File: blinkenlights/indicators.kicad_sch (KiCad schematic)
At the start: 45 parts

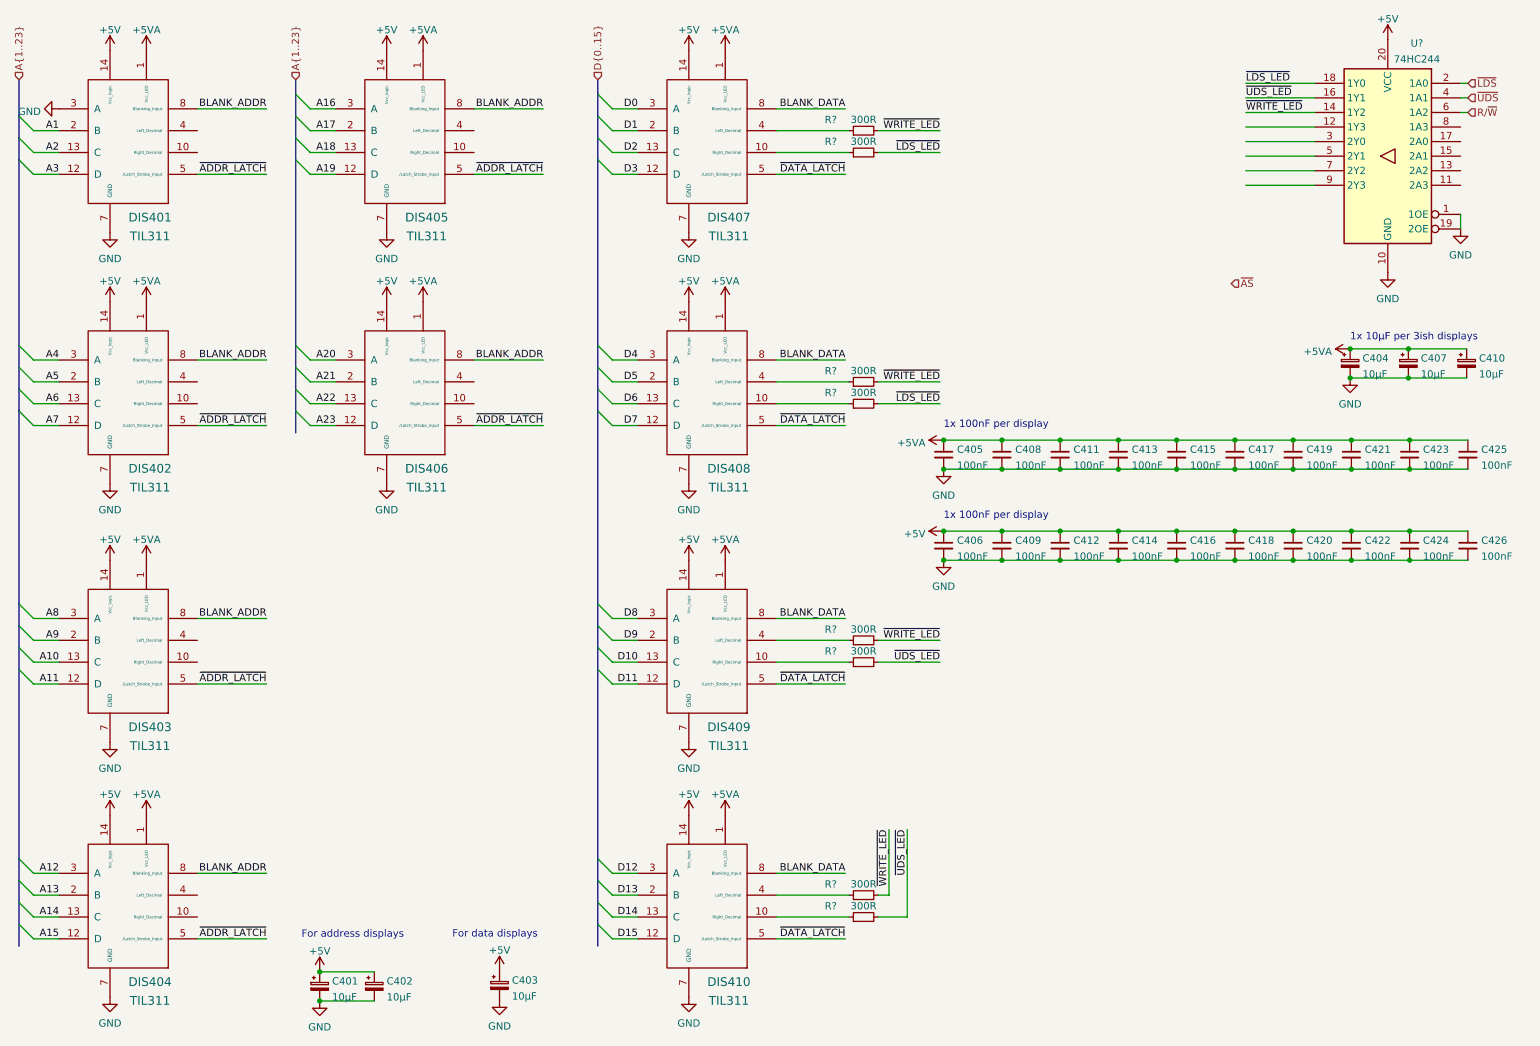
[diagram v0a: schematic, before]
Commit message: Start work on blinkenlights pcb
- This is mostly for the general layout and physical size of the board;
  all the components are placed on the back so the pin numbers will line
  up properly on the DIN connectors.
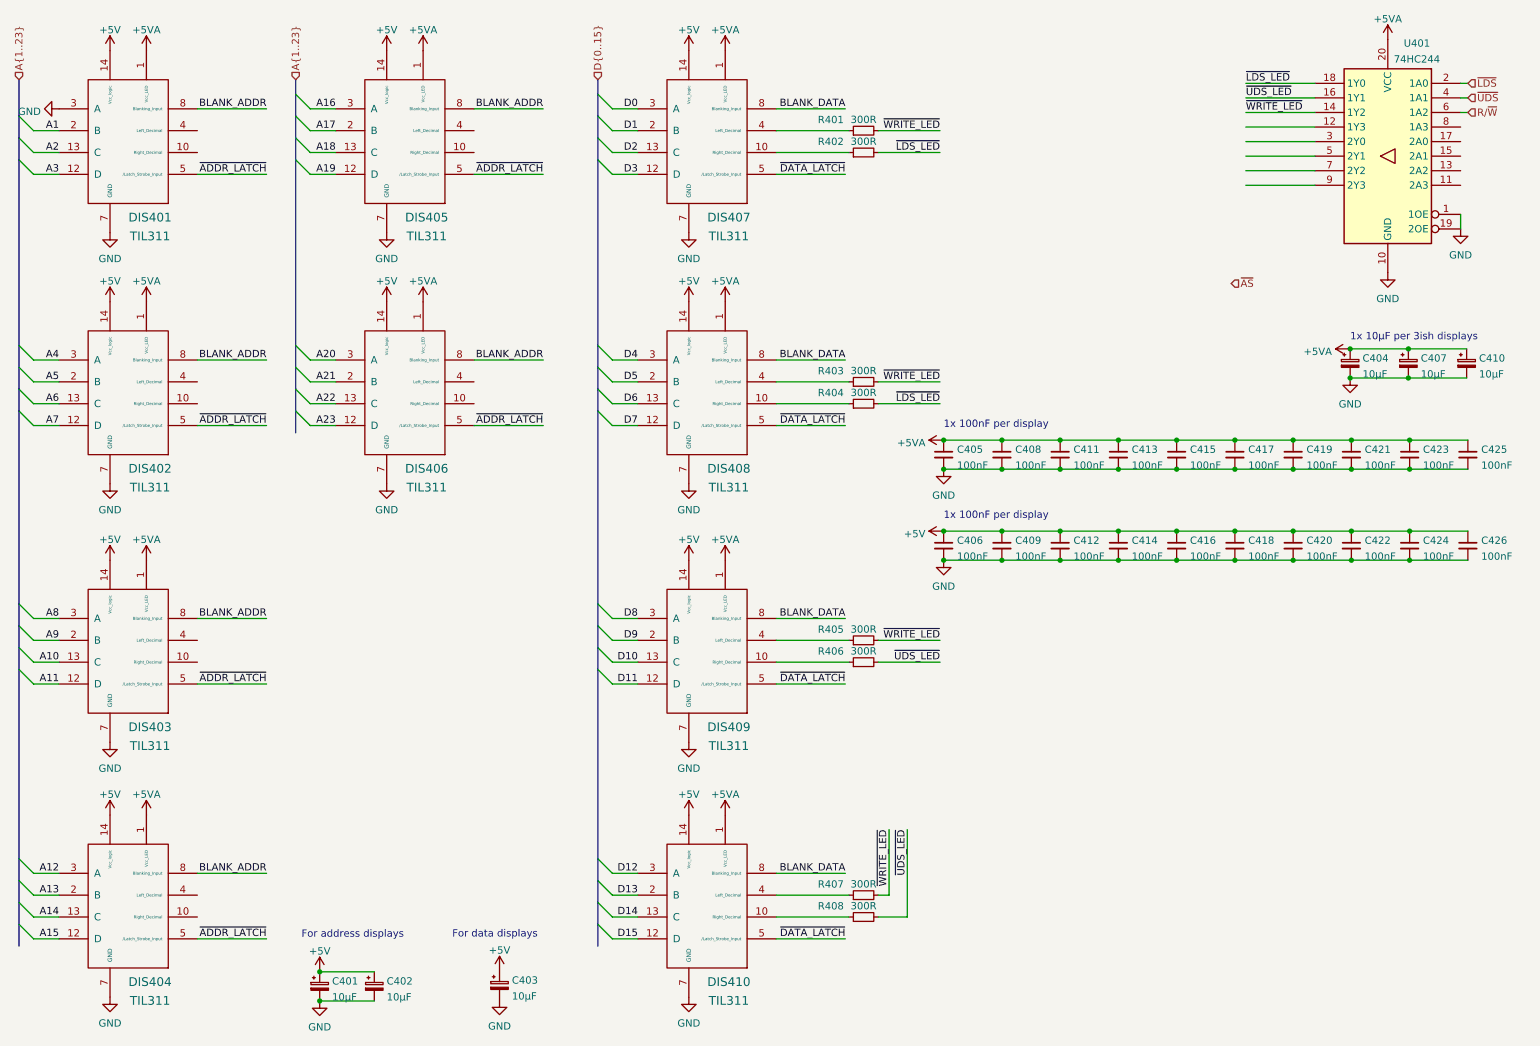
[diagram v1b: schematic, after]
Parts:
- DIS401, DIS402, DIS403, DIS404, DIS405, DIS406, DIS407, DIS408, DIS409, DIS410: footprint (none) -> led-displays-obsolete:TIL311
- R401, R402, R403, R404, R405, R406, R407, R408: renamed from R?; footprint (none) -> Resistor_SMD:R_0805_2012Metric
- gave numbers to parts that had none: 1
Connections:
- net +5V: no longer U401.20 (VCC)
- net +5VA: now also U401.20 (VCC)

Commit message: Added ROM sockets to blinkenlights
- Also started routing some of the IOs and powers for the displays
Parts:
- U401: footprint (none) -> Package_SO:TSSOP-20_4.4x6.5mm_P0.65mm
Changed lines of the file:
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@@
-(kicad_sch (version 20210621) (generator eeschema)
+(kicad_sch (version 20211123) (generator eeschema)
   (paper "A4")
-  (junction (at 191.77 106.045) (diameter 0) (color 0 0 0 0))
-  (junction (at 262.89 95.25) (diameter 0) (color 0 0 0 0))
-  (junction (at 222.25 106.045) (diameter 0) (color 0 0 0 0))
-  (junction (at 252.73 95.25) (diameter 0) (color 0 0 0 0))
-  (junction (at 201.93 95.25) (diameter 0) (color 0 0 0 0))
-  (junction (at 232.41 95.25) (diameter 0) (color 0 0 0 0))
-  (junction (at 262.89 90.17) (diameter 0) (color 0 0 0 0))
-  (junction (at 212.09 95.25) (diameter 0) (color 0 0 0 0))
-  (junction (at 252.73 111.125) (diameter 0) (color 0 0 0 0))
-  (junction (at 212.09 90.17) (diameter 0) (color 0 0 0 0))
-  (junction (at 212.09 106.045) (diameter 0) (color 0 0 0 0))
-  (junction (at 252.73 90.17) (diameter 0) (color 0 0 0 0))
-  (junction (at 181.61 106.045) (diameter 0) (color 0 0 0 0))
-  (junction (at 201.93 106.045) (diameter 0) (color 0 0 0 0))
-  (junction (at 222.25 111.125) (diameter 0) (color 0 0 0 0))
-  (junction (at 181.61 111.125) (diameter 0) (color 0 0 0 0))
-  (junction (at 72.771 187.9984) (diameter 0) (color 0 0 0 0))
-  (junction (at 242.57 95.25) (diameter 0) (color 0 0 0 0))
-  (junction (at 242.57 90.17) (diameter 0) (color 0 0 0 0))
-  (junction (at 262.6741 74.2566) (diameter 0) (color 0 0 0 0))
-  (junction (at 181.61 95.25) (diameter 0) (color 0 0 0 0))
-  (junction (at 222.25 95.25) (diameter 0) (color 0 0 0 0))
-  (junction (at 222.25 90.17) (diameter 0) (color 0 0 0 0))
-  (junction (at 262.89 106.045) (diameter 0) (color 0 0 0 0))
-  (junction (at 72.771 182.9184) (diameter 0) (color 0 0 0 0))
-  (junction (at 201.93 111.125) (diameter 0) (color 0 0 0 0))
-  (junction (at 212.09 111.125) (diameter 0) (color 0 0 0 0))
-  (junction (at 181.61 90.17) (diameter 0) (color 0 0 0 0))
-  (junction (at 232.41 106.045) (diameter 0) (color 0 0 0 0))
-  (junction (at 191.77 95.25) (diameter 0) (color 0 0 0 0))
-  (junction (at 191.77 111.125) (diameter 0) (color 0 0 0 0))
-  (junction (at 252.73 106.045) (diameter 0) (color 0 0 0 0))
-  (junction (at 262.89 111.125) (diameter 0) (color 0 0 0 0))
-  (junction (at 242.57 106.045) (diameter 0) (color 0 0 0 0))
-  (junction (at 191.77 90.17) (diameter 0) (color 0 0 0 0))
-  (junction (at 252.5141 79.3366) (diameter 0) (color 0 0 0 0))
-  (junction (at 201.93 90.17) (diameter 0) (color 0 0 0 0))
-  (junction (at 232.41 111.125) (diameter 0) (color 0 0 0 0))
-  (junction (at 232.41 90.17) (diameter 0) (color 0 0 0 0))
-  (junction (at 242.57 111.125) (diameter 0) (color 0 0 0 0))
-  (junction (at 252.5141 74.2566) (diameter 0) (color 0 0 0 0))
-  (junction (at 262.6741 79.3366) (diameter 0) (color 0 0 0 0))
+  (junction (at 262.89 111.125) (diameter 0) (color 0 0 0 0)
+  )
+  (junction (at 262.89 90.17) (diameter 0) (color 0 0 0 0)
+  )
+  (junction (at 222.25 95.25) (diameter 0) (color 0 0 0 0)
+  )
+  (junction (at 252.73 95.25) (diameter 0) (color 0 0 0 0)
+  )
+  (junction (at 262.6741 79.3366) (diameter 0) (color 0 0 0 0)
+  )
+  (junction (at 252.73 111.125) (diameter 0) (color 0 0 0 0)
+  )
+  (junction (at 201.93 111.125) (diameter 0) (color 0 0 0 0)
+  )
+  (junction (at 232.41 106.045) (diameter 0) (color 0 0 0 0)
+  )
+  (junction (at 212.09 95.25) (diameter 0) (color 0 0 0 0)
+  )
+  (junction (at 222.25 111.125) (diameter 0) (color 0 0 0 0)
+  )
+  (junction (at 201.93 95.25) (diameter 0) (color 0 0 0 0)
+  )
+  (junction (at 242.57 90.17) (diameter 0) (color 0 0 0 0)
+  )
+  (junction (at 181.61 95.25) (diameter 0) (color 0 0 0 0)
+  )
+  (junction (at 181.61 90.17) (diameter 0) (color 0 0 0 0)
+  )
+  (junction (at 252.5141 79.3366) (diameter 0) (color 0 0 0 0)
+  )
+  (junction (at 212.09 111.125) (diameter 0) (color 0 0 0 0)
+  )
+  (junction (at 181.61 111.125) (diameter 0) (color 0 0 0 0)
+  )
+  (junction (at 222.25 106.045) (diameter 0) (color 0 0 0 0)
+  )
+  (junction (at 191.77 111.125) (diameter 0) (color 0 0 0 0)
+  )
+  (junction (at 242.57 95.25) (diameter 0) (color 0 0 0 0)
+  )
+  (junction (at 252.5141 74.2566) (diameter 0) (color 0 0 0 0)
+  )
+  (junction (at 262.89 106.045) (diameter 0) (color 0 0 0 0)
+  )
+  (junction (at 232.41 95.25) (diameter 0) (color 0 0 0 0)
+  )
+  (junction (at 232.41 111.125) (diameter 0) (color 0 0 0 0)
+  )
+  (junction (at 212.09 90.17) (diameter 0) (color 0 0 0 0)
+  )
+  (junction (at 262.6741 74.2566) (diameter 0) (color 0 0 0 0)
+  )
+  (junction (at 72.771 187.9984) (diameter 0) (color 0 0 0 0)
+  )
+  (junction (at 252.73 90.17) (diameter 0) (color 0 0 0 0)
+  )
+  (junction (at 181.61 106.045) (diameter 0) (color 0 0 0 0)
+  )
+  (junction (at 252.73 106.045) (diameter 0) (color 0 0 0 0)
+  )
+  (junction (at 191.77 106.045) (diameter 0) (color 0 0 0 0)
+  )
+  (junction (at 242.57 106.045) (diameter 0) (color 0 0 0 0)
+  )
+  (junction (at 232.41 90.17) (diameter 0) (color 0 0 0 0)
+  )
+  (junction (at 222.25 90.17) (diameter 0) (color 0 0 0 0)
+  )
+  (junction (at 212.09 106.045) (diameter 0) (color 0 0 0 0)
+  )
+  (junction (at 262.89 95.25) (diameter 0) (color 0 0 0 0)
+  )
+  (junction (at 191.77 95.25) (diameter 0) (color 0 0 0 0)
+  )
+  (junction (at 201.93 106.045) (diameter 0) (color 0 0 0 0)
+  )
+  (junction (at 242.57 111.125) (diameter 0) (color 0 0 0 0)
+  )
+  (junction (at 201.93 90.17) (diameter 0) (color 0 0 0 0)
+  )
+  (junction (at 191.77 90.17) (diameter 0) (color 0 0 0 0)
+  )
+  (junction (at 72.771 182.9184) (diameter 0) (color 0 0 0 0)
+  )
   (bus_entry (at 20.32 81.28) (size 2.54 2.54)
     (stroke (width 0) (type default) (color 0 0 0 0))
@@
     (property "Reference" "U401" (id 0) (at 264.16 20.955 0))
     (property "Value" "74HC244" (id 1) (at 264.16 23.7301 0))
-    (property "Footprint" "" (id 2) (at 259.08 40.64 0)
-      (effects (font (size 1.27 1.27)) hide)
-    )
+    (property "Footprint" "Package_SO:TSSOP-20_4.4x6.5mm_P0.65mm" (id 2) (at 259.08 40.64 0)
+      (effects (font (size 1.27 1.27)) hide)
+    )

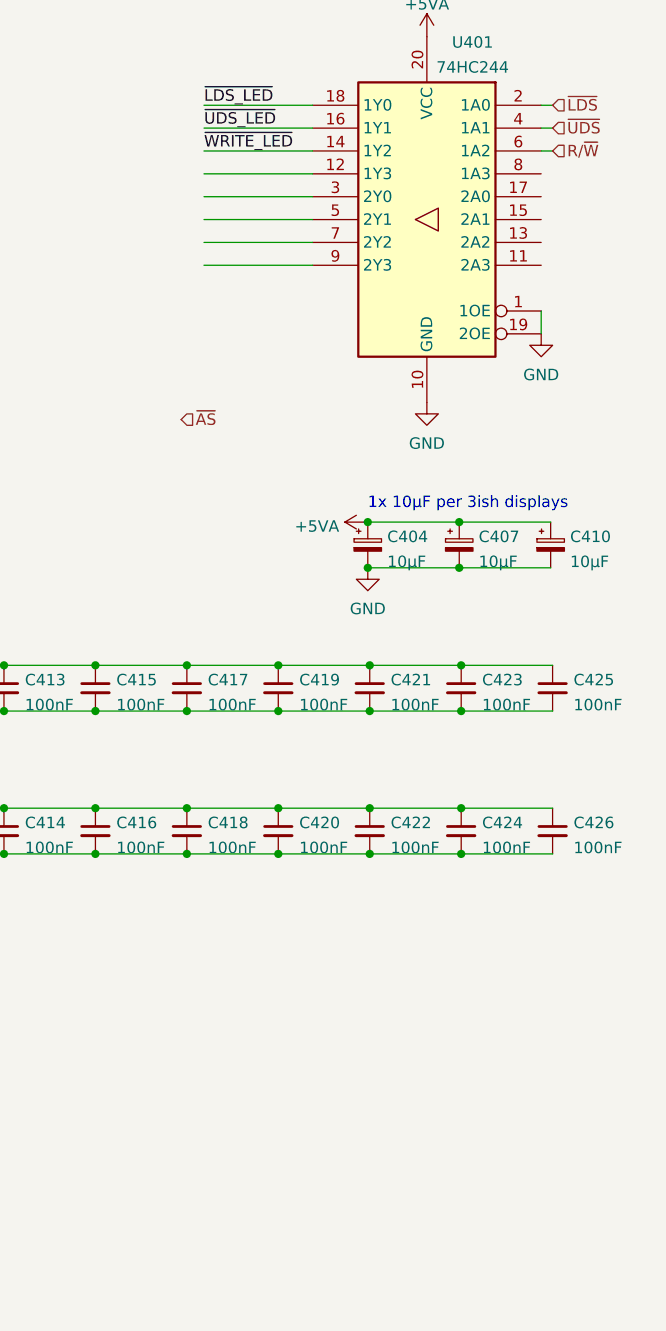
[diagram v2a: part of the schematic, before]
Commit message: Reworked blinkenlights board
- The connector for the CPU board is a female vertical DIN connector
  instead now, which will be a lot less fucky

- Some more LEDs and buttons
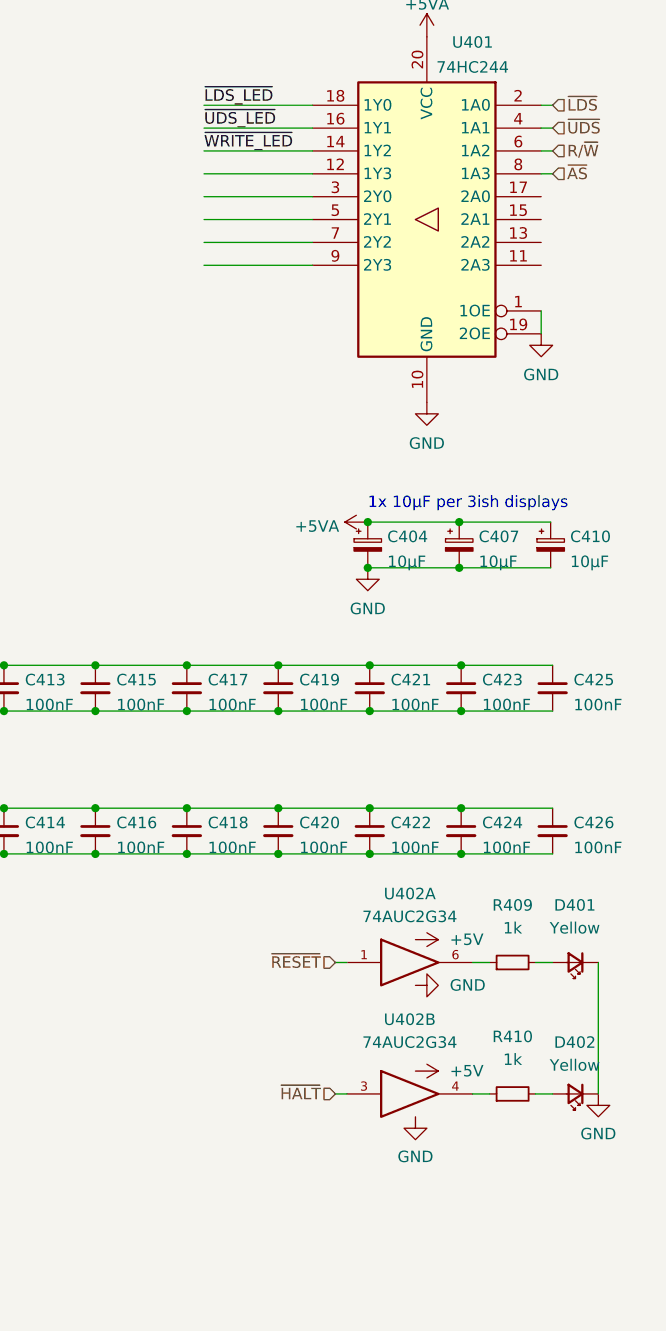
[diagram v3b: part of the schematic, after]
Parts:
- added D401, D402: Yellow, LED_SMD:LED_0805_2012Metric, symbol Device:LED_Small
- added R409, R410: 1k, Resistor_SMD:R_0805_2012Metric, symbol Device:R_Small
- added U402: 74AUC2G34, Package_TO_SOT_SMD:SOT-23-6, symbol 74xGxx:74AUC2G34
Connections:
- net +5V: now also U402.5 (VCC), U402.5 (VCC)
- net GND: now also D401.1 (K), D402.1 (K), U402.2 (GND), U402.2 (GND)
- net ~{AS}: now also U401.8 (1A3)
- new net: R409.1, U402.6
- new net: D401.2 (A), R409.2
- new net: R410.1, U402.4
- new net: D402.2 (A), R410.2
- new net ~{HALT}: U402.3
- new net ~{RESET}: U402.1
